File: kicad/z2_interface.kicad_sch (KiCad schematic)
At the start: 0 parts

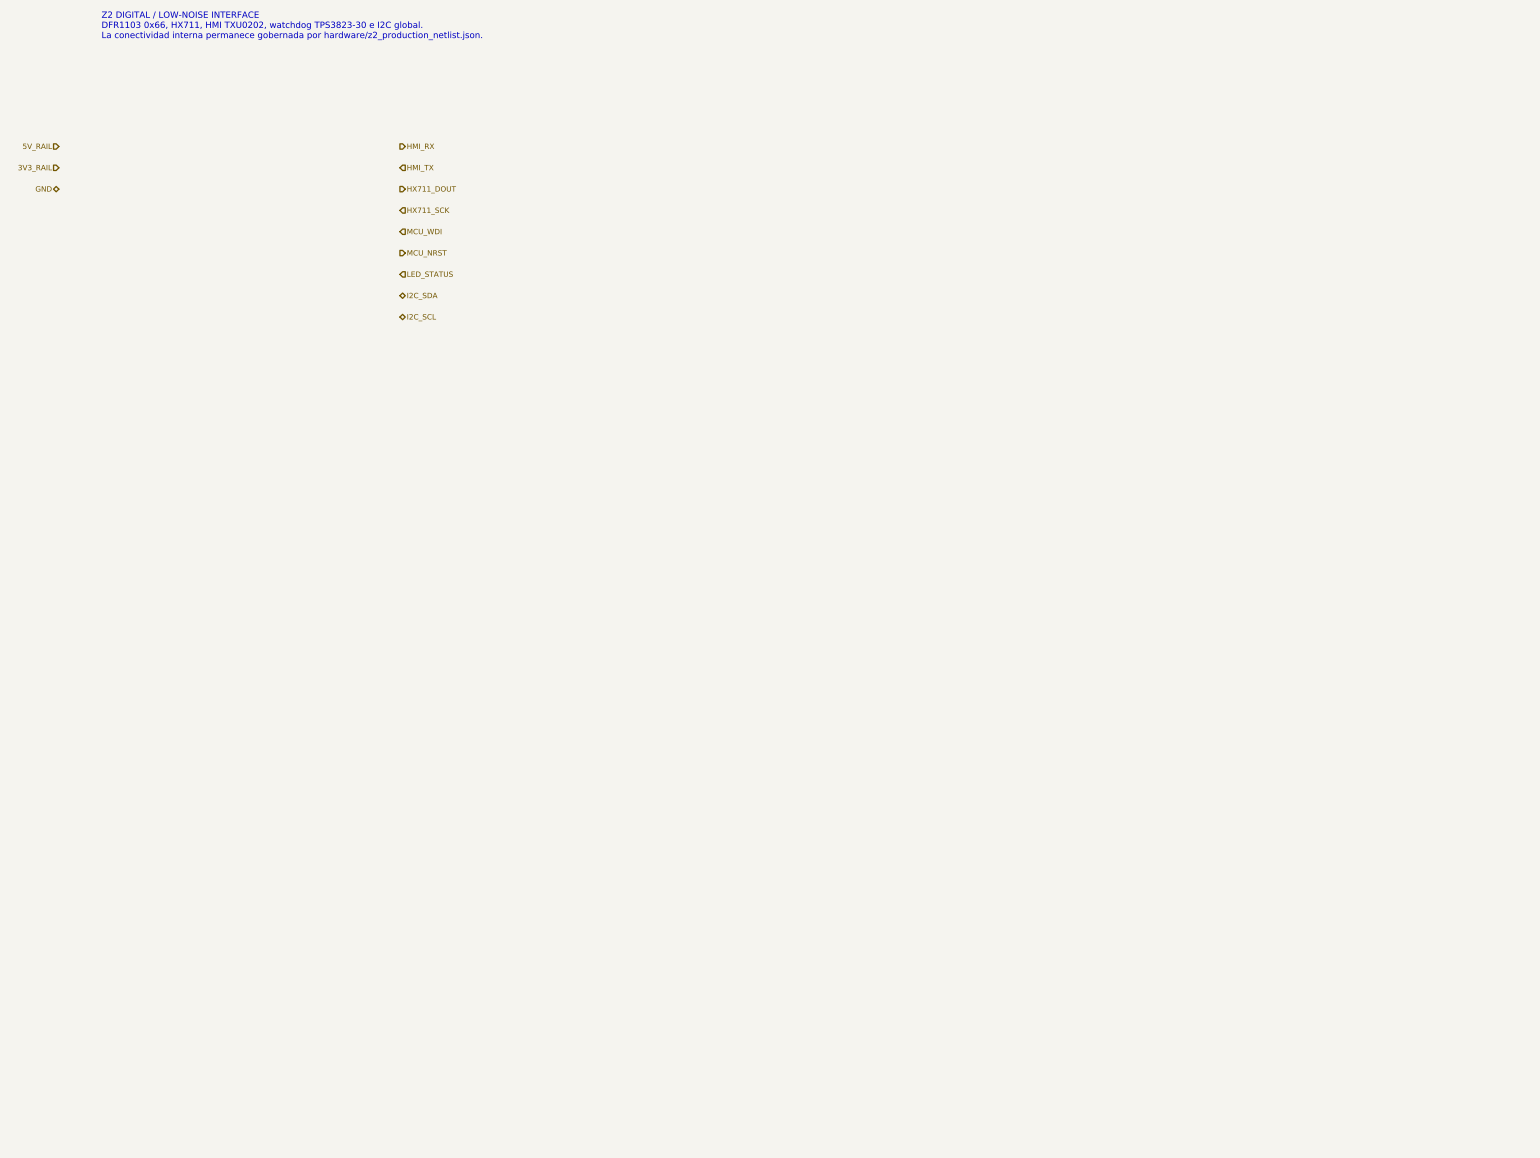
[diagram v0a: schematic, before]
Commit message: eda: materializar hojas de producción Z0-Z4 PR15
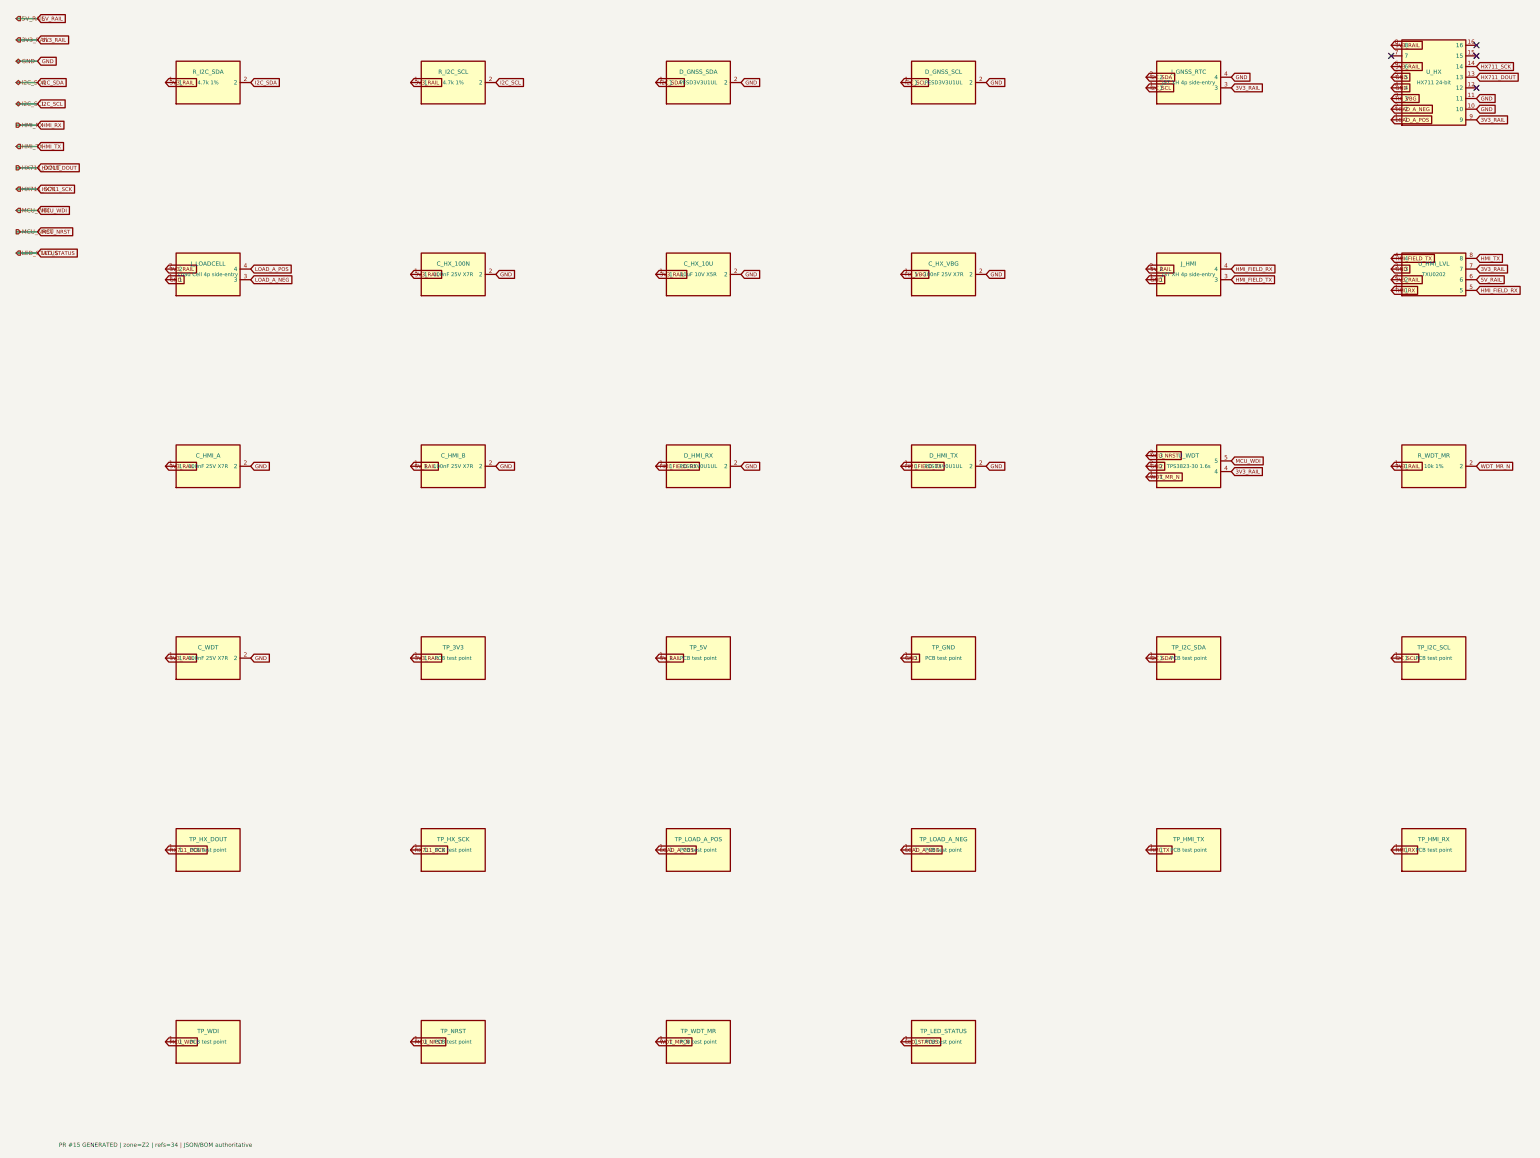
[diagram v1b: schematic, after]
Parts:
- added C_HMI_A: 100nF 25V X7R, Capacitor_SMD:C_0402_1005Metric, symbol NFB_GEN:SYM_C_HMI_A
- added C_HMI_B: 100nF 25V X7R, Capacitor_SMD:C_0402_1005Metric, symbol NFB_GEN:SYM_C_HMI_B
- added C_HX_100N: 100nF 25V X7R, Capacitor_SMD:C_0402_1005Metric, symbol NFB_GEN:SYM_C_HX_100N
- added C_HX_10U: 10uF 10V X5R, Capacitor_SMD:C_0805_2012Metric, symbol NFB_GEN:SYM_C_HX_10U
- added C_HX_VBG: 100nF 25V X7R, Capacitor_SMD:C_0402_1005Metric, symbol NFB_GEN:SYM_C_HX_VBG
- added C_WDT: 100nF 25V X7R, Capacitor_SMD:C_0402_1005Metric, symbol NFB_GEN:SYM_C_WDT
- added D_GNSS_SCL: PESD3V3U1UL, Diode_SMD:D_SOD-882, symbol NFB_GEN:SYM_D_GNSS_SCL
- added D_GNSS_SDA: PESD3V3U1UL, Diode_SMD:D_SOD-882, symbol NFB_GEN:SYM_D_GNSS_SDA
- added D_HMI_RX: PESD5V0U1UL, Diode_SMD:D_SOD-882, symbol NFB_GEN:SYM_D_HMI_RX
- added D_HMI_TX: PESD5V0U1UL, Diode_SMD:D_SOD-882, symbol NFB_GEN:SYM_D_HMI_TX
- added J_GNSS_RTC: JST XH 4p side-entry, Connector_JST:JST_XH_S4B-XH-A_1x04_P2.50mm_Horizontal, symbol NFB_GEN:SYM_J_GNSS_RTC
- added J_HMI: JST XH 4p side-entry, Connector_JST:JST_XH_S4B-XH-A_1x04_P2.50mm_Horizontal, symbol NFB_GEN:SYM_J_HMI
- added J_LOADCELL: Load Cell 4p side-entry, TerminalBlock_Phoenix:TerminalBlock_Phoenix_PT-1,5-4-5.0-H_1x04_P5.00mm_Horizontal, symbol NFB_GEN:SYM_J_LOADCELL
- added R_I2C_SCL: 4.7k 1%, Resistor_SMD:R_0402_1005Metric, symbol NFB_GEN:SYM_R_I2C_SCL
- added R_I2C_SDA: 4.7k 1%, Resistor_SMD:R_0402_1005Metric, symbol NFB_GEN:SYM_R_I2C_SDA
- added R_WDT_MR: 10k 1%, Resistor_SMD:R_0402_1005Metric, symbol NFB_GEN:SYM_R_WDT_MR
- added TP_3V3: PCB test point, TestPoint:TestPoint_Pad_D1.0mm, symbol NFB_GEN:SYM_TP_3V3
- added TP_5V: PCB test point, TestPoint:TestPoint_Pad_D1.0mm, symbol NFB_GEN:SYM_TP_5V
- added TP_GND: PCB test point, TestPoint:TestPoint_Pad_D1.0mm, symbol NFB_GEN:SYM_TP_GND
- added TP_HMI_RX: PCB test point, TestPoint:TestPoint_Pad_D1.0mm, symbol NFB_GEN:SYM_TP_HMI_RX
- added TP_HMI_TX: PCB test point, TestPoint:TestPoint_Pad_D1.0mm, symbol NFB_GEN:SYM_TP_HMI_TX
- added TP_HX_DOUT: PCB test point, TestPoint:TestPoint_Pad_D1.0mm, symbol NFB_GEN:SYM_TP_HX_DOUT
- added TP_HX_SCK: PCB test point, TestPoint:TestPoint_Pad_D1.0mm, symbol NFB_GEN:SYM_TP_HX_SCK
- added TP_I2C_SCL: PCB test point, TestPoint:TestPoint_Pad_D1.0mm, symbol NFB_GEN:SYM_TP_I2C_SCL
- added TP_I2C_SDA: PCB test point, TestPoint:TestPoint_Pad_D1.0mm, symbol NFB_GEN:SYM_TP_I2C_SDA
- added TP_LED_STATUS: PCB test point, TestPoint:TestPoint_Pad_D1.0mm, symbol NFB_GEN:SYM_TP_LED_STATUS
- added TP_LOAD_A_NEG: PCB test point, TestPoint:TestPoint_Pad_D1.0mm, symbol NFB_GEN:SYM_TP_LOAD_A_NEG
- added TP_LOAD_A_POS: PCB test point, TestPoint:TestPoint_Pad_D1.0mm, symbol NFB_GEN:SYM_TP_LOAD_A_POS
- added TP_NRST: PCB test point, TestPoint:TestPoint_Pad_D1.0mm, symbol NFB_GEN:SYM_TP_NRST
- added TP_WDI: PCB test point, TestPoint:TestPoint_Pad_D1.0mm, symbol NFB_GEN:SYM_TP_WDI
- added TP_WDT_MR: PCB test point, TestPoint:TestPoint_Pad_D1.0mm, symbol NFB_GEN:SYM_TP_WDT_MR
- added U_HMI_LVL: TXU0202, Package_MSOP:VSSOP-8_2x3.1mm_P0.65mm, symbol NFB_GEN:SYM_U_HMI_LVL
- added U_HX: HX711 24-bit, Package_SO:SOP-16_4.4x10.4mm_P1.27mm, symbol NFB_GEN:SYM_U_HX
- added U_WDT: TPS3823-30 1.6s, Package_TO_SOT_SMD:SOT-23-5, symbol NFB_GEN:SYM_U_WDT
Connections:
- net 3V3_RAIL: now also C_HMI_A.1, C_HX_100N.1, C_HX_10U.1, C_WDT.1, J_GNSS_RTC.3, J_LOADCELL.2, R_I2C_SCL.1, R_I2C_SDA.1, R_WDT_MR.1, TP_3V3.1, U_HMI_LVL.2, U_HMI_LVL.7, U_HX.6, U_HX.8, U_HX.9, U_WDT.4
- net 5V_RAIL: now also C_HMI_B.1, J_HMI.2, TP_5V.1, U_HMI_LVL.6
- net GND: now also C_HMI_A.2, C_HMI_B.2, C_HX_100N.2, C_HX_10U.2, C_HX_VBG.2, C_WDT.2, D_GNSS_SCL.2, D_GNSS_SDA.2, D_HMI_RX.2, D_HMI_TX.2, J_GNSS_RTC.4, J_HMI.1, J_LOADCELL.1, TP_GND.1, U_HMI_LVL.3, U_HX.10, U_HX.11, U_HX.4, U_HX.5, U_WDT.2
- net HMI_RX: now also TP_HMI_RX.1, U_HMI_LVL.1
- net HMI_TX: now also TP_HMI_TX.1, U_HMI_LVL.8
- net HX711_DOUT: now also TP_HX_DOUT.1, U_HX.13
- net HX711_SCK: now also TP_HX_SCK.1, U_HX.14
- net I2C_SCL: now also D_GNSS_SCL.1, J_GNSS_RTC.1, R_I2C_SCL.2, TP_I2C_SCL.1
- net I2C_SDA: now also D_GNSS_SDA.1, J_GNSS_RTC.2, R_I2C_SDA.2, TP_I2C_SDA.1
- net LED_STATUS: now also TP_LED_STATUS.1
- net MCU_NRST: now also TP_NRST.1, U_WDT.3
- net MCU_WDI: now also TP_WDI.1, U_WDT.5
- new net HMI_FIELD_RX: D_HMI_RX.1, J_HMI.4, U_HMI_LVL.5
- new net HMI_FIELD_TX: D_HMI_TX.1, J_HMI.3, U_HMI_LVL.4
- new net HX_VBG: C_HX_VBG.1, U_HX.3
- new net LOAD_A_NEG: J_LOADCELL.3, TP_LOAD_A_NEG.1, U_HX.2
- new net LOAD_A_POS: J_LOADCELL.4, TP_LOAD_A_POS.1, U_HX.1
- new net WDT_MR_N: R_WDT_MR.2, TP_WDT_MR.1, U_WDT.1
- no-connect marks 0 -> 4
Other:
- note added: "PR #15 GENERATED | zone=Z2 | refs=34 | JSON/BOM authoritative"
- note removed: "Z2 DIGITAL / LOW-NOISE INTERFACE DFR1103 0x66, HX711, HMI TXU0202, watchdog TPS3823-30 e I2C global. La conectividad interna permanece gobernada por hardware/z2_production_netlist.json."
- title: NFB Insight PCBA v2 — Z2 Interface -> NFB Insight PCBA v2 — Z2 GENERATED PRODUCTION
